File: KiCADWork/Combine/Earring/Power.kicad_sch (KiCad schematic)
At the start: 10 parts, among them U1 MCP73831T-2ACI/OT, U2 XB6096I2SV

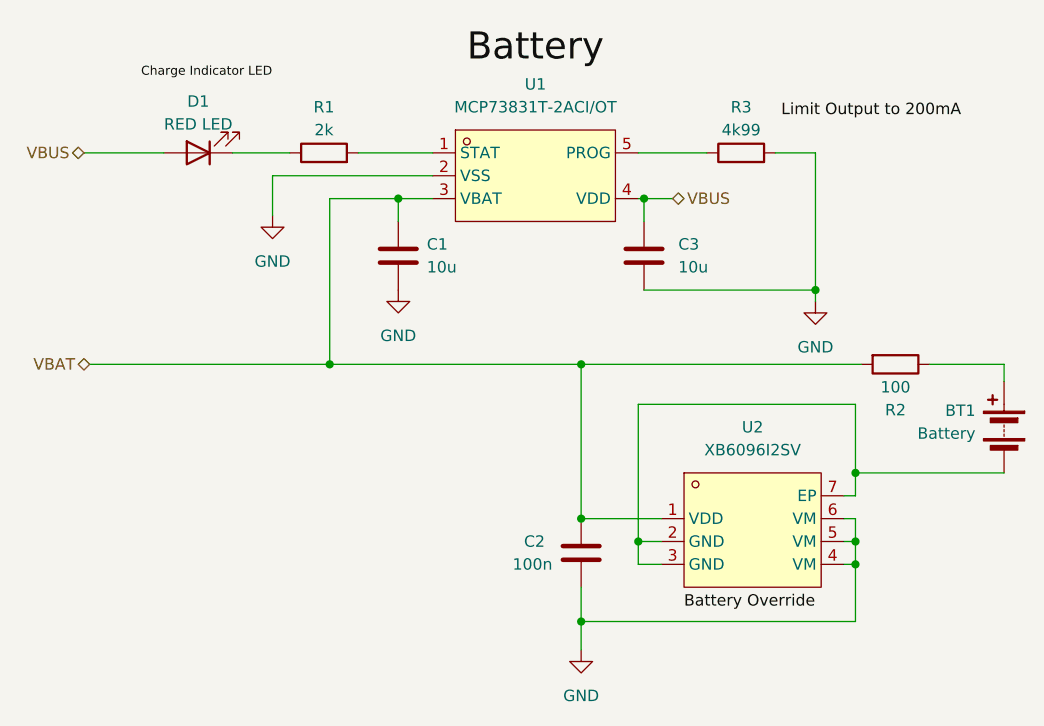
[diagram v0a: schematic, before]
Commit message: Completing the combined layout
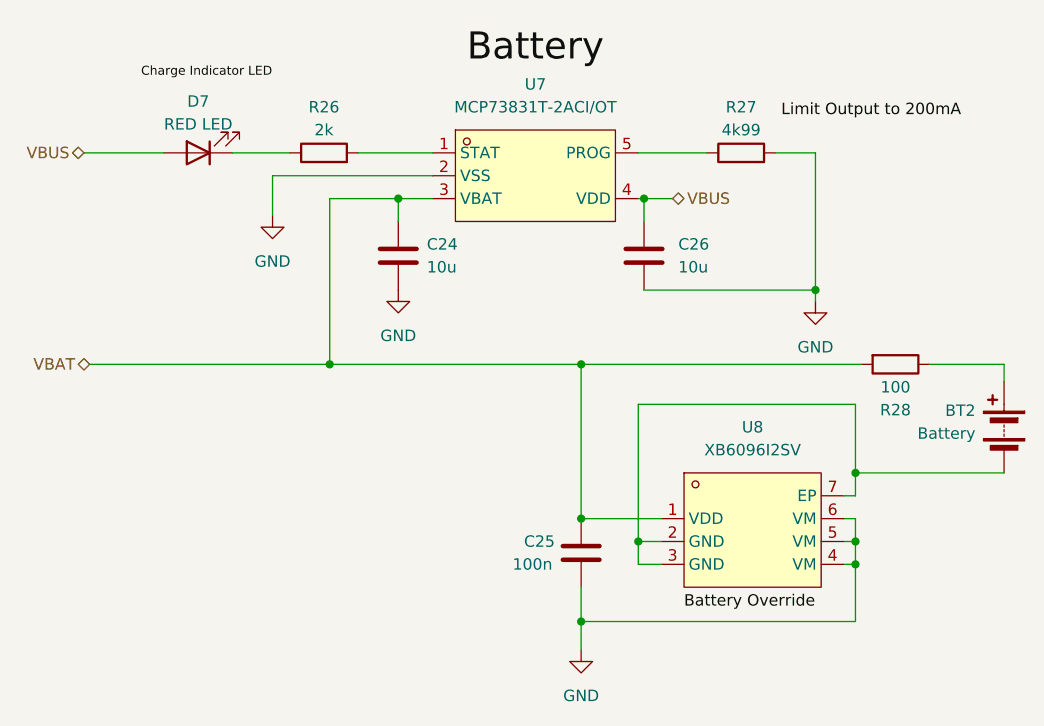
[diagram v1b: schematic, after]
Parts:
- renumbered BT1 to BT2, C1 to C24, C2 to C25, C3 to C26, D1 to D7, R1 to R26, R3 to R27, R2 to R28, U1 to U7, U2 to U8
